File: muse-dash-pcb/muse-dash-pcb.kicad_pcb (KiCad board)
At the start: 2 copper layers, 84.1 x 51.3 mm, 33 parts, among them J1 AVR-ISP-6, SW0 SW_Push, SW1 CherryMX, SW2 CherryMX, SW3 CherryMX, SW4 CherryMX, U1 ATmega32U4-A, Y1 Crystal_GND24

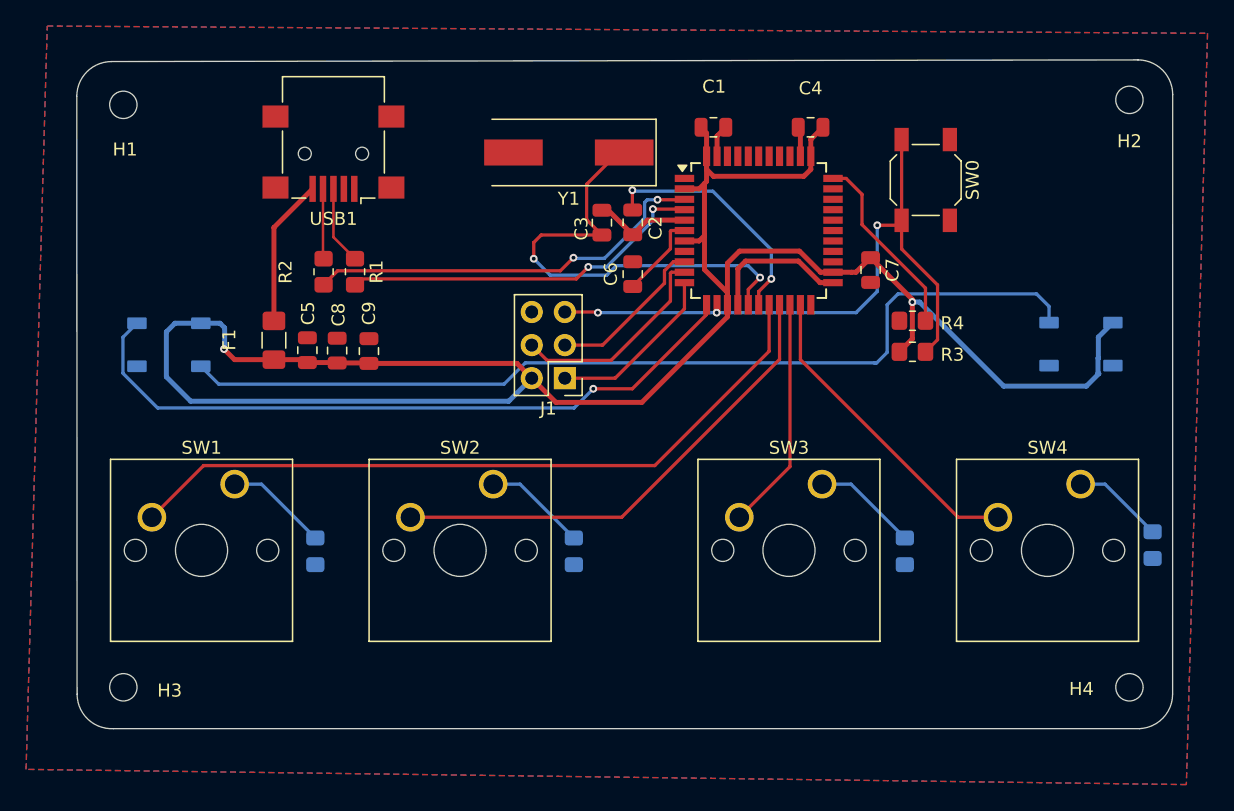
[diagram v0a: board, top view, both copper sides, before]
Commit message: silkscreen text added
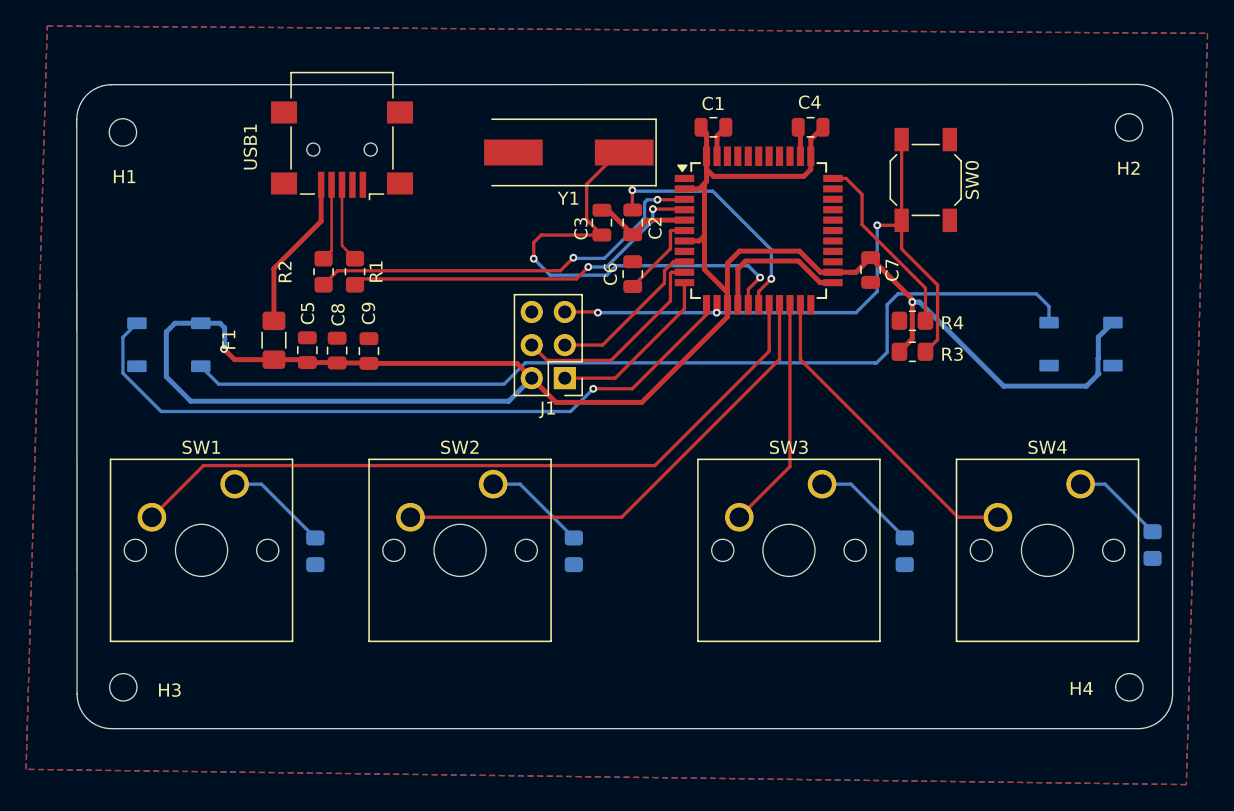
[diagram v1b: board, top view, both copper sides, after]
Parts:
- moved H1 2.12 mm to (156.7, 57.0)
- moved H2 2.12 mm to (233.9, 56.6)
- moved USB1 0.73 mm to (173.5, 58.3)
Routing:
- net VCC: track 11.4 -> 11.9 mm
- net D-: track 5.38 -> 5.93 mm
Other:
- board size 84.1 x 51.3 mm -> 84.1 x 49.4 mm
- board text added: "/$$ /$$ | $$ |__/ | $$$$$$$ /$$$$$$ /$$$$$$/$$$$ /$$ /$$$$$$$ /$$ /$$ /$$$$$$/$$$$ | $$__ $$ /$$__ $$| $$_ $$_ $$| $$| $$__ $$| $$ | $$| $$_ $$_ $$ | $$ \ $$| $$ \ $$| $$ \ $$ \ $$| $$| $$ \ $$| $$ | $$| $$ \ $$ \ $$ | $$ | $$| $$ | $$| $$ | $$ | $$| $$| $$ | $$| $$ | $$| $$ | $$ | $$ | $$ | $$| $$$$$$/| $$ | $$ | $$| $$| $$ | $$| $$$$$$/| $$ | $$ | $$ |__/ |__/ \______/ |__/ |__/ |__/|__/|__/ |_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"
- board text added: "Muse Dash Keypad"
- board text removed: "@hominum0447"

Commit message: inverted text color
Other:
- board text added: "@hominum0447"
- board text removed: "/$$ /$$ | $$ |__/ | $$$$$$$ /$$$$$$ /$$$$$$/$$$$ /$$ /$$$$$$$ /$$ /$$ /$$$$$$/$$$$ | $$__ $$ /$$__ $$| $$_ $$_ $$| $$| $$__ $$| $$ | $$| $$_ $$_ $$ | $$ \ $$| $$ \ $$| $$ \ $$ \ $$| $$| $$ \ $$| $$ | $$| $$ \ $$ \ $$ | $$ | $$| $$ | $$| $$ | $$ | $$| $$| $$ | $$| $$ | $$| $$ | $$ | $$ | $$ | $$| $$$$$$/| $$ | $$ | $$| $$| $$ | $$| $$$$$$/| $$ | $$ | $$ |__/ |__/ \______/ |__/ |__/ |__/|__/|__/ |_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"
